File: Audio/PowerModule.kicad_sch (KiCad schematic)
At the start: 15 parts, among them J4 PWR_IN, J5 PWR_OUT, U1 TEC 3-1223

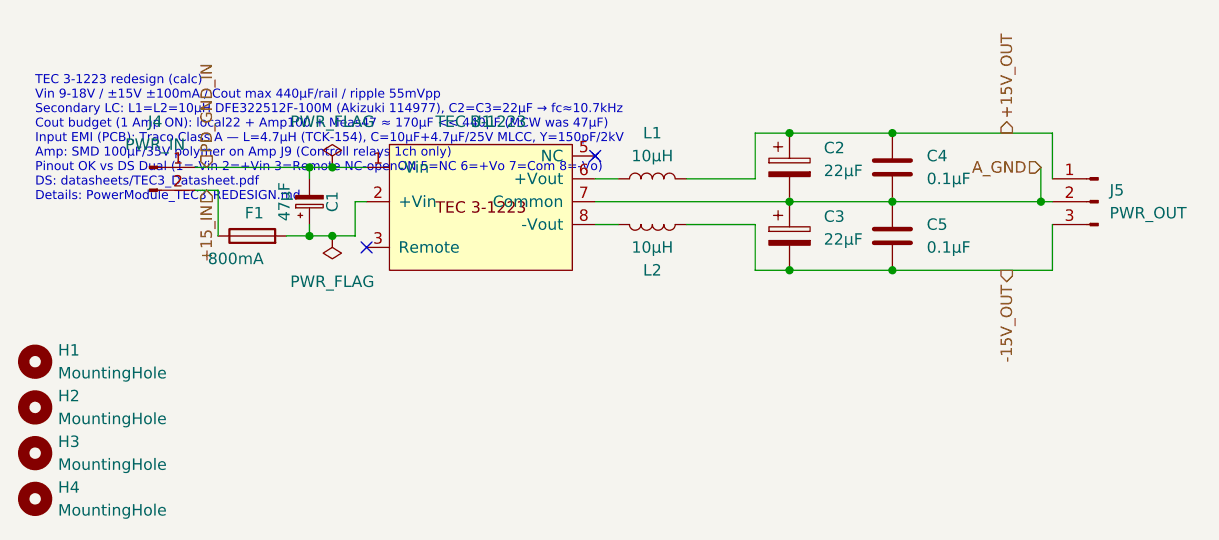
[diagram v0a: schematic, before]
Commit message: TEC 3では電流不足のため PowerModule を TMR 6-1223 にする (#13)
* PowerModuleのU1をTMR 6-1223にし、TEC 3単体の電流不足を解消する。

TEC 3はCoutは足りるが±100mAのままなので、Amp複数・Controllなし・
DIP差し替えでは危険。同じSIP-8 DualのTMR 6（±200mA、Cout 660µF）に
載せ、F1をDS推奨の1.6A遅断にする。

Co-authored-by: m_arino <indare@users.noreply.github.com>

* TMR 6の上（TMR 9 / TMR 12WI）は電流は増えるが Cout が減ると明記する。

TMR 9 は ±300mA だが Cout 200µF、ケースピンがあり本 FP に直挿しできない。
電流増が要るなら単体の段上げではなく Amp 用の 2 台目にする。

Co-authored-by: m_arino <indare@users.noreply.github.com>

* PowerModuleはSIP互換を捨てて15W級（REC15 / DKA15）を本命にする。

TMR 9/12は電流は増えるがCoutが減る。基板再設計可なら2インチ×1インチの
±500mA・Cout 680〜1000µFを取る。

Co-authored-by: m_arino <indare@users.noreply.github.com>

* 再設計候補に DKMW20/30（1インチ角で電流とCoutを両立）を追加する。

Co-authored-by: m_arino <indare@users.noreply.github.com>

* 12V入力のDKA15をAサフィックスに直し、SIP-8の国内代替を追記する。

Co-authored-by: m_arino <indare@users.noreply.github.com>

* Mean Well DPB09はSIP-8でもCout 47µFなので使わないと明記する。

Co-authored-by: m_arino <indare@users.noreply.github.com>

* 再設計候補に THN 30-1223（1インチ角・±1A・Cout 500µF）を追加する。

Co-authored-by: m_arino <indare@users.noreply.github.com>

---------

Co-authored-by: Cursor Agent <cursoragent@cursor.com>
Co-authored-by: m_arino <indare@users.noreply.github.com>
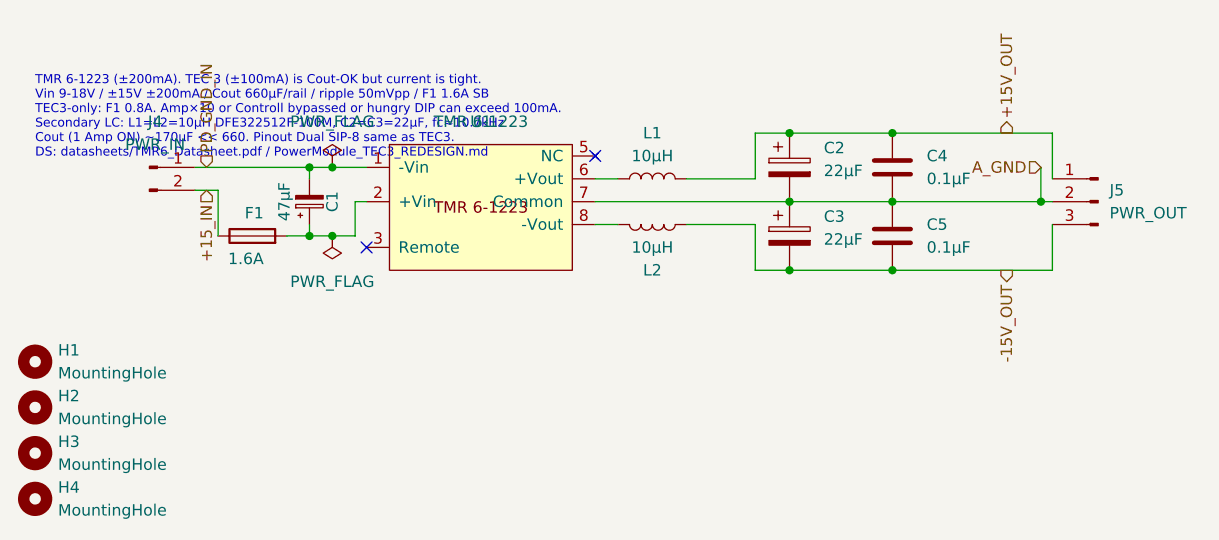
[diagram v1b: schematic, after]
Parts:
- F1: value 800mA -> 1.6A
- U1: value TEC 3-1223 -> TMR 6-1223; MPN TEC 3-1223 -> TMR 6-1223
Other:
- note added: "TMR 6-1223 (±200mA). TEC 3 (±100mA) is Cout-OK but current is tight. Vin 9-18V / ±15V ±200mA / Cout 660µF/rail / ripple 50mVpp / F1 1.6A SB TEC3-only: F1 0.8A. Amp×10 or Controll bypassed or hungry DIP can exceed 100mA. Secondary LC: L1=L2=10µH DFE322512F-100M, C2=C3=22µF, fc≈10.7kHz Cout (1 Amp ON) ~170µF << 660. Pinout Dual SIP-8 same as TEC3. DS: datasheets/TMR6_Datasheet.pdf / PowerModule_TEC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"
- note removed: "TEC 3-1223 redesign (calc) Vin 9-18V / ±15V ±100mA / Cout max 440µF/rail / ripple 55mVpp Secondary LC: L1=L2=10µH DFE322512F-100M (Akizuki 114977), C2=C3=22µF → fc≈10.7kHz Cout budget (1 Amp ON): local22 + Amp100 + Meas47 ≈ 170µF << 440µF (MCW was 47µF) Input EMI (PCB): Traco Class A — L=4.7µH (TCK-154), C=10µF+4.7µF/25V MLCC, Y=150pF/2kV Amp: SMD 100µF/35V polymer on Amp J9 (Controll relays 1ch 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"
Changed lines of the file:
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@@
 		)
 	)
-	(text "TEC 3-1223 redesign (calc)\nVin 9-18V / ±15V ±100mA / Cout max 440µF/rail / ripple 55mVpp\nSecondary LC: L1=L2=10µH DFE322512F-100M (Akizuki 114977), C2=C3=22µF → fc≈10.7kHz\nCout budget (1 Amp ON): local22 + Amp100 + Meas47 ≈ 170µF << 440µF (MCW was 47µF)\nInput EMI (PCB): Traco Class A — L=4.7µH (TCK-154), C=10µF+4.7µF/25V MLCC, Y=150pF/2kV\nAmp: SMD 100µF/35V polymer on Amp J9 (Controll relays 1ch only)\nPinout OK vs DS Dual (1=-Vin 2=+Vin 3=Remote NC-openON 5=NC 6=+Vo 7=Com 8=-Vo)\nDS: datasheets/TEC3_Datasheet.pdf\nDetails: PowerModule_TEC3_REDESIGN.md"
+	(text "TMR 6-1223 (±200mA). TEC 3 (±100mA) is Cout-OK but current is tight.\nVin 9-18V / ±15V ±200mA / Cout 660µF/rail / ripple 50mVpp / F1 1.6A SB\nTEC3-only: F1 0.8A. Amp×10 or Controll bypassed or hungry DIP can exceed 100mA.\nSecondary LC: L1=L2=10µH DFE322512F-100M, C2=C3=22µF, fc≈10.7kHz\nCout (1 Amp ON) ~170µF << 660. Pinout Dual SIP-8 same as TEC3.\nDS: datasheets/TMR6_Datasheet.pdf / PowerModule_TEC3_REDESIGN.md"
 		(exclude_from_sim no)
 		(at 15.24 26.67 0)
@@
 			)
 		)
-		(property "Value" "TEC 3-1223"
+		(property "Value" "TMR 6-1223"
 			(at 64.77 31.75 0)
 			(show_name no)
@@
 			)
 		)
-		(property "Datasheet" "https://www.tracopower.com/sites/default/files/products/datasheets/tec3_datasheet.pdf"
+		(property "Datasheet" "https://www.tracopower.com/sites/default/files/products/datasheets/tmr6_datasheet.pdf"
 			(at 65.278 29.972 0)
 			(hide yes)
@@
 			)
 		)
-		(property "Description" "Traco TEC 3-1223; DS: datasheets/TEC3_Datasheet.pdf / https://www.tracopower.com/sites/default/files/products/datasheets/tec3_datasheet.pdf; pins verified Dual SIP-8"
+		(property "Description" "Traco TMR 6-1223 ±15V/±200mA SIP-8; same Dual pinout as TEC 3-1223; DS: datasheets/TMR6_Datasheet.pdf"
 			(at 64.77 31.75 0)
 			(hide yes)
@@
 			)
 		)
-		(property "MPN" "TEC 3-1223"
+		(property "MPN" "TMR 6-1223"
 			(at 64.77 31.75 0)
 			(hide yes)
@@
 			)
 		)
-		(property "Value" "800mA"
+		(property "Value" "1.6A"
 			(at 40.64 46.99 90)
 			(show_name no)
@@
 			)
 		)
-		(property "Description" "Traco TEC3-12xx recommended input fuse 0.8A slow-blow"
+		(property "Description" "Traco TMR 6-12xx recommended input fuse 1.6A slow-blow (TEC 3-12xx was 0.8A)"
 			(at 39.37 44.45 0)
 			(hide yes)
